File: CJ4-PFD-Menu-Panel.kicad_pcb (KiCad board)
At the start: 2 copper layers, 122.4 x 62.5 mm, 0 parts

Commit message: Some board layout work
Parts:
- added C1: 100nF, Custom_Footprints:Perfect_0402, B.Cu at (64.3, 26.5)
- added C10: 100nF, Custom_Footprints:Perfect_0402, B.Cu at (74.9, 23.7)
- added C11: 100nF, Custom_Footprints:Perfect_0402, B.Cu at (79.0, 26.2)
- added C12: 1uF, Custom_Footprints:Perfect_0402, B.Cu at (90.6, 42.4)
- added C13: 100nF, Custom_Footprints:Perfect_0402, B.Cu at (86.6, 37.9)
- added C14: 1uF, Custom_Footprints:Perfect_0402, B.Cu at (87.5, 40.4)
- added C15: 100nF, Custom_Footprints:Perfect_0402, B.Cu at (81.8, 34.4)
- added C16: 100nF, Custom_Footprints:Perfect_0402, B.Cu at (84.9, 32.0)
- added C17: 100nF, Custom_Footprints:Perfect_0402, B.Cu at (101.1, 45.1)
- added C18: 100nF, Custom_Footprints:Perfect_0402, B.Cu at (98.0, 45.1)
- added C19: 100nF, Custom_Footprints:Perfect_0402, B.Cu at (80.9, 28.3)
- added C20: 100nF, Custom_Footprints:Perfect_0402, B.Cu at (77.7, 28.3)
- added C5: 10pF, Custom_Footprints:Perfect_0402, B.Cu at (90.6, 40.4)
- added C6: 10pF, Custom_Footprints:Perfect_0402, B.Cu at (80.9, 30.3)
- added C7: 10uF, Capacitor_SMD:C_0603_1608Metric, B.Cu at (90.2, 38.1)
- added C8: 100nF, Custom_Footprints:Perfect_0402, B.Cu at (94.8, 45.1)
- added C9: 10uF, Capacitor_SMD:C_0603_1608Metric, B.Cu at (84.5, 29.8)
- added H1: Board mount, MountingHole:MountingHole_3.2mm_M3, F.Cu at (25.0, 25.0)
- added H10: JLCPCB tooling, Custom_Footprints:JLCPCB_Tooling_Hole, B.Cu at (30.0, 25.0)
- added H2: Board mount, MountingHole:MountingHole_3.2mm_M3, F.Cu at (137.0, 25.0)
- added H3: Board mount, MountingHole:MountingHole_3.2mm_M3, F.Cu at (25.0, 72.0)
- added H4: Board mount, MountingHole:MountingHole_3.2mm_M3, F.Cu at (137.0, 72.0)
- added H5: BARO encoder, Custom_Footprints:EN11-HSM1BF20_PM, F.Cu at (43.0, 52.0)
- added H6: MENU ADV and DATA encoder, Custom_Footprints:EC11E-BB24C03_PM, F.Cu at (81.0, 52.0)
- added H7: TILT and RANGE encoder, Custom_Footprints:EC11E-BB24C03_PM, F.Cu at (119.0, 52.0)
- added H8: JLCPCB tooling, Custom_Footprints:JLCPCB_Tooling_Hole, B.Cu at (132.0, 25.0)
- added H9: JLCPCB tooling, Custom_Footprints:JLCPCB_Tooling_Hole, B.Cu at (132.0, 72.0)
- added J1: USB_B_Micro, Custom_Footprints:USB_B_Mini_Amphenol_UE25BE5510H, B.Cu at (96.6, 32.1)
- added J2: Conn_01x03, Connector_PinHeader_2.54mm:PinHeader_1x03_P2.54mm_Vertical, B.Cu at (88.8, 25.0)
- added J3: BARO encoder, Connector_JST:JST_XH_B5B-XH-A_1x05_P2.50mm_Vertical, B.Cu at (48.0, 70.5)
- added J4: MENU ADV and DATA encoder, Connector_JST:JST_XH_B8B-XH-A_1x08_P2.50mm_Vertical, B.Cu at (89.8, 70.5)
- added J5: TILT and RANGE encoder, Connector_JST:JST_XH_B8B-XH-A_1x08_P2.50mm_Vertical, B.Cu at (127.2, 70.5)
- added J6: Conn_01x02, Connector_JST:JST_XH_B2B-XH-A_1x02_P2.50mm_Vertical, B.Cu at (100.8, 70.5)
- added J7: Conn_01x02, Connector_JST:JST_XH_B2B-XH-A_1x02_P2.50mm_Vertical, B.Cu at (60.8, 70.5)
- added R1: 1k, Custom_Footprints:Perfect_0402, B.Cu at (85.0, 34.1)
- added R2: 1k, Custom_Footprints:Perfect_0402, B.Cu at (74.9, 25.8)
- added R3: DNF, Resistor_SMD:R_1206_3216Metric_Pad1.30x1.75mm_HandSolder, B.Cu at (83.5, 24.4)
- added R4: 27, Resistor_SMD:R_0603_1608Metric, B.Cu at (78.5, 24.0)
- added R5: 27, Resistor_SMD:R_0603_1608Metric, B.Cu at (84.5, 27.3)
- added R6: 10k, Custom_Footprints:Perfect_0402, B.Cu at (81.8, 32.4)
- added R7: R_Small, Custom_Footprints:Perfect_0402, B.Cu at (67.5, 26.5)
- added SW1: SW_Push, Button_Switch_SMD:SW_SPST_TL3342, B.Cu at (107.0, 34.1)
- added SW10: SW_PUSH_LED, Custom_Footprints:SW_PUSH_LED_SMD, F.Cu at (60.0, 45.0)
- added SW11: SW_PUSH_LED, Custom_Footprints:SW_PUSH_LED_SMD, F.Cu at (60.0, 59.0)
- added SW12: SW_PUSH_LED, Custom_Footprints:SW_PUSH_LED_SMD, F.Cu at (102.0, 45.0)
- added SW13: SW_PUSH_LED, Custom_Footprints:SW_PUSH_LED_SMD, F.Cu at (102.0, 59.0)
- added SW2: SW_Push, Button_Switch_SMD:SW_SPST_TL3342, B.Cu at (107.0, 26.5)
- added SW3: SW_PUSH_LED, Custom_Footprints:SW_PUSH_LED_SMD, F.Cu at (39.0, 30.0)
- added SW4: SW_PUSH_LED, Custom_Footprints:SW_PUSH_LED_SMD, F.Cu at (53.0, 30.0)
- added SW5: SW_PUSH_LED, Custom_Footprints:SW_PUSH_LED_SMD, F.Cu at (67.0, 30.0)
- added SW6: SW_PUSH_LED, Custom_Footprints:SW_PUSH_LED_SMD, F.Cu at (81.0, 30.0)
- added SW7: SW_PUSH_LED, Custom_Footprints:SW_PUSH_LED_SMD, F.Cu at (95.0, 30.0)
- added SW8: SW_PUSH_LED, Custom_Footprints:SW_PUSH_LED_SMD, F.Cu at (109.0, 30.0)
- added SW9: SW_PUSH_LED, Custom_Footprints:SW_PUSH_LED_SMD, F.Cu at (123.0, 30.0)
- added TP1: TestPoint, TestPoint:TestPoint_Keystone_5000-5004_Miniature, B.Cu at (-11.5, 24.5)
- added TP2: TestPoint, TestPoint:TestPoint_Keystone_5000-5004_Miniature, B.Cu at (-22.0, 28.5)
- added TP3: TestPoint, TestPoint:TestPoint_Keystone_5000-5004_Miniature, B.Cu at (-15.8, 31.5)
- added TP4: TestPoint, TestPoint:TestPoint_Keystone_5000-5004_Miniature, B.Cu at (-11.5, 31.5)
- added TP5: TestPoint, TestPoint:TestPoint_Keystone_5000-5004_Miniature, B.Cu at (-15.8, 24.5)
- added U1: AMS1117-3.3, Package_TO_SOT_SMD:SOT-223-3_TabPin2, B.Cu at (107.6, 42.0)
- added U2: DM13A, Package_SO:SSOP-24_3.9x8.7mm_P0.635mm, B.Cu at (57.2, 29.2)
- added U5: W25Q128JVS, Package_SO:SOIC-8_5.23x5.23mm_P1.27mm, B.Cu at (96.3, 26.1)
- added U6: RP2040, Custom_Footprints:QFN-56-1EP_7x7mm_P0.4mm_EP3.2x3.2mm, B.Cu at (96.8, 39.4)
- added Y1: X322512MSB4SI, Crystal:Crystal_SMD_3225-4Pin_3.2x2.5mm, B.Cu at (89.2, 34.6)
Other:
- board size 122.4 x 62.5 mm -> 122 x 57 mm

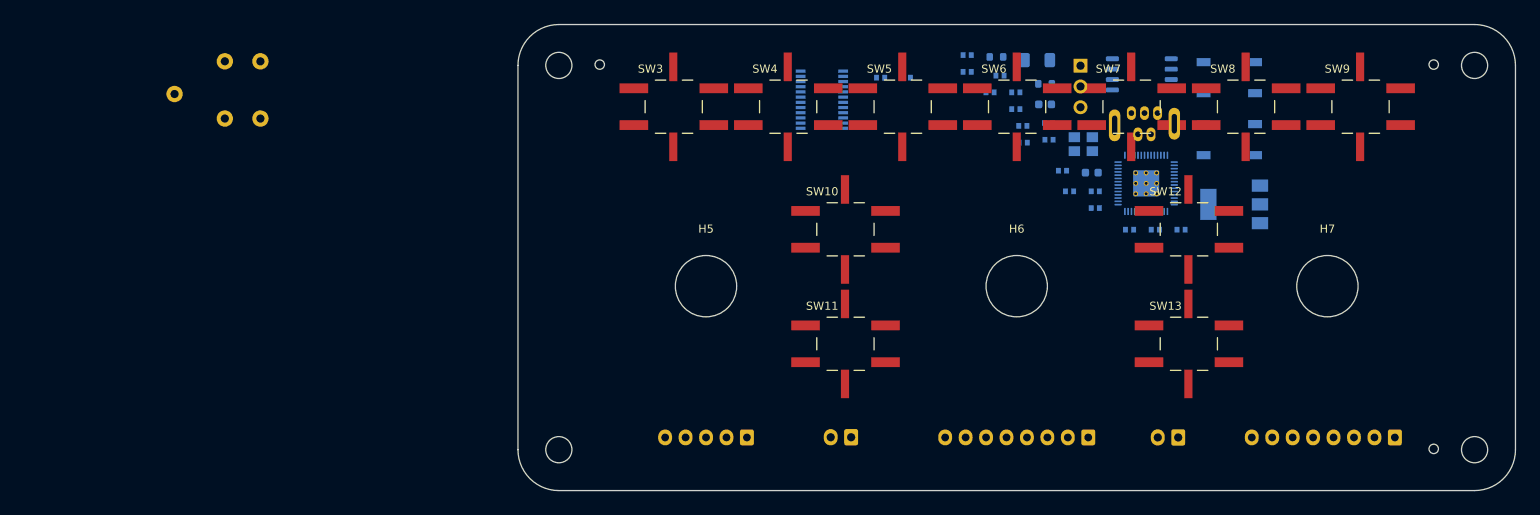
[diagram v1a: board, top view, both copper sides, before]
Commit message: Redo RP2040 layout
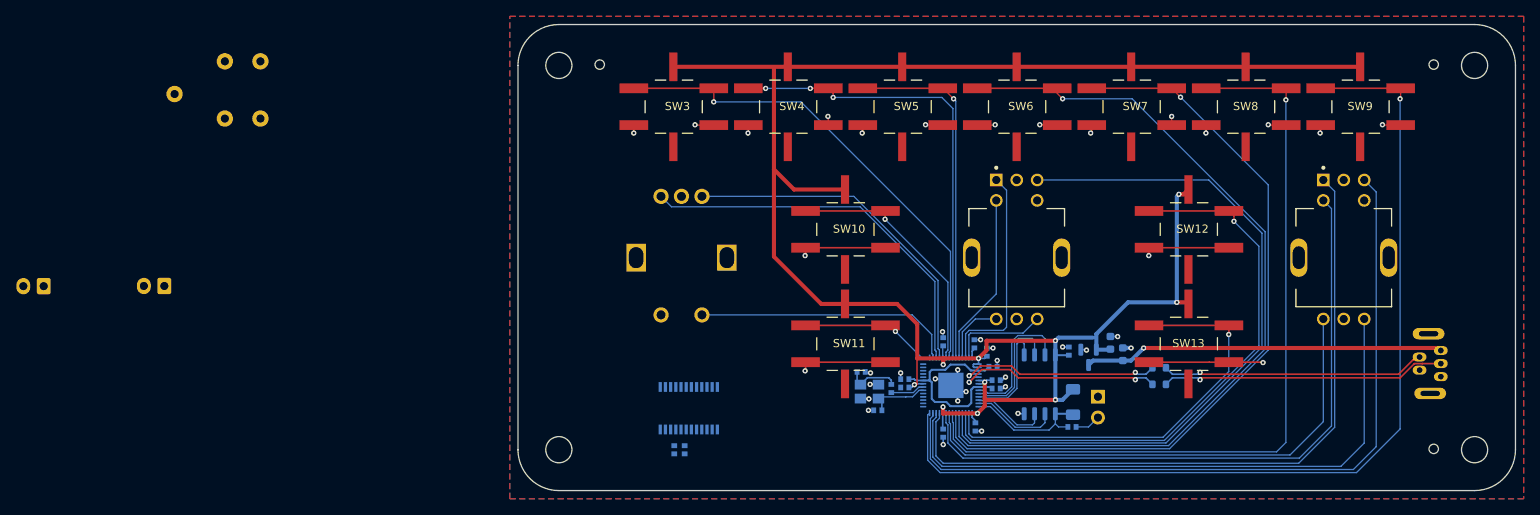
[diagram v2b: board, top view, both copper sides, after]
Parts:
- removed C14: 1uF, Custom_Footprints:Perfect_0402
- removed H5: BARO encoder, Custom_Footprints:EN11-HSM1BF20_PM
- removed H6: MENU ADV and DATA encoder, Custom_Footprints:EC11E-BB24C03_PM
- removed H7: TILT and RANGE encoder, Custom_Footprints:EC11E-BB24C03_PM
- removed J2: Conn_01x03, Connector_PinHeader_2.54mm:PinHeader_1x03_P2.54mm_Vertical
- removed J4: MENU ADV and DATA encoder, Connector_JST:JST_XH_B8B-XH-A_1x08_P2.50mm_Vertical
- removed J5: TILT and RANGE encoder, Connector_JST:JST_XH_B8B-XH-A_1x08_P2.50mm_Vertical
- removed J7: Conn_01x02, Connector_JST:JST_XH_B2B-XH-A_1x02_P2.50mm_Vertical
- removed R4: 27, Resistor_SMD:R_0603_1608Metric
- removed SW1, SW2: SW_Push, Button_Switch_SMD:SW_SPST_TL3342
- removed U5: W25Q128JVS, Package_SO:SOIC-8_5.23x5.23mm_P1.27mm
- added ENC1: BARO encoder, Custom_Footprints:EN11-HSM1BF20_THT, F.Cu at (40.0, 48.5)
- added ENC2: MENU ADV and DATA encoder, Custom_Footprints:ALPS-EC11EBB24C03-0, F.Cu at (81.0, 48.5)
- added ENC3: TILT and RANGE encoder, Custom_Footprints:ALPS-EC11EBB24C03-0, F.Cu at (121.0, 48.5)
- added J8: Conn_01x02, Connector_JST:JST_XH_B2B-XH-A_1x02_P2.50mm_Vertical, B.Cu at (-38.0, 52.0)
- added U7: RP2040, Custom_Footprints:QFN57P40_700X700X90L40X18T310N, B.Cu at (72.9, 64.1)
- C10, C11, C13, C15, C16, C17, C18, C19, C20: value 100nF -> 1uF
- C7, C9: value 10uF -> 1uF
- J1: value USB_B_Micro -> Conn_01x02; footprint Custom_Footprints:USB_B_Mini_Amphenol_UE25BE5510H -> Connector_JST:JST_XH_B2B-XH-A_1x02_P2.50mm_Vertical
- J3: value BARO encoder -> Conn_01x02; footprint Connector_JST:JST_XH_B5B-XH-A_1x05_P2.50mm_Vertical -> Connector_PinHeader_2.54mm:PinHeader_1x02_P2.54mm_Vertical
- J6: value Conn_01x02 -> USB_B_Micro; footprint Connector_JST:JST_XH_B2B-XH-A_1x02_P2.50mm_Vertical -> Custom_Footprints:USB_B_Mini_Amphenol_UE25BE5510H
- R1: value 1k -> R_Small
- R3: value DNF -> 1k; footprint Resistor_SMD:R_1206_3216Metric_Pad1.30x1.75mm_HandSolder -> Custom_Footprints:Perfect_0402
- R5: value 27 -> DNF; footprint Resistor_SMD:R_0603_1608Metric -> Resistor_SMD:R_1206_3216Metric_Pad1.30x1.75mm_HandSolder
- R6: value 10k -> 27; footprint Custom_Footprints:Perfect_0402 -> Resistor_SMD:R_0603_1608Metric
- R7: value R_Small -> 27; footprint Custom_Footprints:Perfect_0402 -> Resistor_SMD:R_0603_1608Metric
- U1: value AMS1117-3.3 -> DM13A; footprint Package_TO_SOT_SMD:SOT-223-3_TabPin2 -> Package_SO:SSOP-24_3.9x8.7mm_P0.635mm
- U2: value DM13A -> XC6206P332MR; footprint Package_SO:SSOP-24_3.9x8.7mm_P0.635mm -> Package_TO_SOT_SMD:SOT-23
- U6: value RP2040 -> W25Q128JVS; footprint Custom_Footprints:QFN-56-1EP_7x7mm_P0.4mm_EP3.2x3.2mm -> Package_SO:SOIC-8_5.23x5.23mm_P1.27mm
- moved J1 121.5 mm to (-23.2, 52.0)
- moved U1 71.2 mm to (40.9, 66.9), turned to 90 degrees
- moved R1 59.5 mm to (39.1, 72.0), turned to 90 degrees
- moved C1 51.4 mm to (40.4, 72.0), turned to 90 degrees
- moved R7 47.1 mm to (98.4, 62.0)
- moved U2 45.3 mm to (89.8, 60.7), turned to -90 degrees
- moved R3 45.1 mm to (87.8, 69.2), turned to 0 degrees
- moved J3 43.2 mm to (90.9, 65.5)
- moved C19 41.2 mm to (75.9, 69.2), turned to -90 degrees
- moved Y1 40.0 mm to (63.0, 64.9), turned to 0 degrees
- moved R2 39.8 mm to (65.7, 64.5), turned to 90 degrees
- moved R5 39.1 mm to (87.9, 66.2), turned to -90 degrees
- moved C17 38.3 mm to (72.0, 70.0), turned to -90 degrees
- moved C11 38.3 mm to (78.5, 64.5), turned to 0 degrees
- moved C10 38.2 mm to (78.1, 61.8), turned to 0 degrees
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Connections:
- J1 pad 1: VBUS -> /MASTER_WARNING
- J1 pad 2: /RP2040/USB_D- -> GND
- J3 pad 1: /BARO_A -> GND
- J3 pad 2: GND -> /RP2040/~{USB_BOOT}
- J6 pad 1: /MASTER_WARNING -> VBUS
- J6 pad 2: GND -> /RP2040/USB_D-
- R1 pad 1: /RP2040/QSPI_SS -> /REXT
- R1 pad 2: /RP2040/~{USB_BOOT} -> GND
- R3 pad 1: +3V3 -> /RP2040/QSPI_SS
- R3 pad 2: /RP2040/QSPI_SS -> /RP2040/~{USB_BOOT}
- R5 pad 1: /RP2040/USB_D- -> +3V3
- R5 pad 2: /RP2040/USB_D-R -> /RP2040/QSPI_SS
- R6 pad 1: /RP2040/RUN -> /RP2040/USB_D+
- R6 pad 2: +3V3 -> /RP2040/USB_D_R+
- R7 pad 1: Net-(R7-Pad1) -> /RP2040/USB_D-
- R7 pad 2: GND -> /RP2040/USB_D_R-
- U1 pad 2: +3V3 -> /LED_DIN
- U1 pad 3: VBUS -> /LED_CLOCK
- U2 pad 2: /LED_DIN -> +3V3
- U2 pad 3: /LED_CLOCK -> VBUS
- U6 pad 1: +3V3 -> /RP2040/QSPI_SS
- U6 pad 2: /LED_DIN -> /RP2040/QSPI_SD1
- U6 pad 3: /LED_CLOCK -> /RP2040/QSPI_SD2
- U6 pad 4: /LED_LATCH -> GND
- U6 pad 5: /BRIGHTNESS -> /RP2040/QSPI_SD0
- U6 pad 6: /MASTER_WARNING -> /RP2040/QSPI_SCLK
- U6 pad 7: /MASTER_CAUTION -> /RP2040/QSPI_SD3
- U6 pad 8: /NAV -> +3V3
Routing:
- net +3V3: track 0.00 -> 246.4 mm, vias 0 -> 10
- net /TFC: track 0.00 -> 118.0 mm, vias 0 -> 1
- net /ET: track 0.00 -> 102.8 mm, vias 0 -> 1
- net /TERRWX: track 0.00 -> 98.1 mm, vias 0 -> 1
- net /RANGE_B': track 0.00 -> 95.2 mm
- net /FRMT: track 0.00 -> 93.4 mm, vias 0 -> 1
- net /DATA_B': track 0.00 -> 88.7 mm
- net /TILT_A': track 0.00 -> 87.2 mm
- net GND: track 0.00 -> 86.8 mm, vias 0 -> 40
- net /AUTO_TILT_BTN: track 0.00 -> 81.1 mm
- net /RANGE_B: track 0.00 -> 75.1 mm
- net /RADAR_MENU: track 0.00 -> 71.4 mm, vias 0 -> 1
- net /TILT_A: track 0.00 -> 64.0 mm
- net /NAV: track 0.00 -> 61.0 mm, vias 0 -> 1
- net /PFD_MENU: track 0.00 -> 56.9 mm, vias 0 -> 3
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- added copper zone on B.Cu, net GND
- added copper zone on F.Cu, net GND

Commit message: Fully routed!
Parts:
- J1, J8: footprint Connector_JST:JST_XH_B2B-XH-A_1x02_P2.50mm_Vertical -> Connector_JST:JST_XH_B3B-XH-A_1x03_P2.50mm_Vertical
- SW10, SW11, SW12, SW13, SW3, SW4, SW5, SW6, SW7, SW8, SW9: footprint Custom_Footprints:SW_PUSH_LED_SMD -> Custom_Footprints:SW_PUSH_LED_THT
- moved TP2 94.3 mm to (61.1, 73.2)
- moved TP1 91.7 mm to (66.2, 73.2)
- moved TP3 83.1 mm to (56.0, 73.2)
- moved TP5 79.4 mm to (46.7, 73.4)
- moved TP4 78.1 mm to (58.3, 66.5)
- moved J8 64.1 mm to (25.4, 42.8), turned to 90 degrees
- moved J1 48.7 mm to (25.4, 54.4), turned to 90 degrees
- moved C1 15.5 mm to (51.7, 61.5)
- moved R1 15.5 mm to (50.4, 61.5)
- moved U1 6.40 mm to (47.2, 66.2)
- moved J6 4.70 mm to (130.0, 65.9)
- moved C6 2.61 mm to (60.2, 64.4), turned to -90 degrees
- moved R6 2.55 mm to (98.2, 66.5)
- moved R7 2.55 mm to (98.2, 64.5)
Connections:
- J1 pad 1: /MASTER_WARNING -> /LED_CAUTION
- J1 pad 2: GND -> /MASTER_WARNING
- J8 pad 1: /MASTER_CAUTION -> /LED_WARNING
- J8 pad 2: GND -> /MASTER_CAUTION
- U1 pad 10: /LED_TERRWX -> /LED_WARNING
- U1 pad 11: /LED_TFC -> /LED_CAUTION
- U1 pad 12: /LED_CCP_MENU -> /LED_NAV
- U1 pad 13: /LED_TAWS_MENU -> /LED_PFD_MENU
- U1 pad 14: /LED_RADAR_MENU -> /LED_ESC
- U1 pad 15: /LED_REFS_MENU -> /LED_ET
- U1 pad 16: /LED_MASTER_CAUTION -> /LED_FRMT
- U1 pad 17: /LED_MASTER_WARNING -> /LED_TERRWX
- U1 pad 18: unconnected-(U1-Pad18) -> /LED_RADAR_MENU
- U1 pad 19: unconnected-(U1-Pad19) -> /LED_REFS_MENU
- U1 pad 20: unconnected-(U1-Pad20) -> /LED_CCP_MENU
- U1 pad 5: /LED_NAV -> /LED_TAWS_MENU
- U1 pad 6: /LED_PFD_MENU -> /LED_TFC
- U1 pad 7: /LED_ESC -> unconnected-(U1-Pad7)
- U1 pad 8: /LED_ET -> unconnected-(U1-Pad8)
- U1 pad 9: /LED_FRMT -> unconnected-(U1-Pad9)
- U7 pad 11: /TILT_A' -> /TILT_A
- U7 pad 12: /RANGE_B -> /RANGE_B'
- U7 pad 13: /RANGE_B' -> /RANGE_B
- U7 pad 15: /RP2040/GPIO12 -> /LED_DIN
- U7 pad 16: /RP2040/GPIO13 -> /LED_CLOCK
- U7 pad 17: /RP2040/GPIO14 -> /LED_LATCH
- U7 pad 18: /RP2040/GPIO15 -> /BRIGHTNESS
- U7 pad 27: /RP2040/GPIO16 -> /MASTER_WARNING
- U7 pad 28: /RP2040/GPIO17 -> /MASTER_CAUTION
- U7 pad 29: /REFS_MENU -> /STD_BTN
- U7 pad 3: /RADAR_MENU -> /DATA_B'
- U7 pad 30: /STD_BTN -> /REFS_MENU
- U7 pad 31: /BARO_B -> /CCP_MENU
- U7 pad 34: /CCP_MENU -> /BARO_B
- U7 pad 38: /SELECT_BTN -> /MENU_ADV_A'
- U7 pad 39: /MENU_ADV_A -> /SELECT_BTN
- U7 pad 4: /DATA_B' -> /RADAR_MENU
- U7 pad 40: /MENU_ADV_A' -> /MENU_ADV_A
- U7 pad 8: /TILT_A -> /TILT_A'
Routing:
- net /LED_TFC: track 0.00 -> 116.5 mm, vias 0 -> 2
- net /LED_TERRWX: track 0.00 -> 88.9 mm, vias 0 -> 4
- net /LED_RADAR_MENU: track 0.00 -> 83.4 mm, vias 0 -> 4
- net /LED_FRMT: track 0.00 -> 76.1 mm, vias 0 -> 4
- net /LED_TAWS_MENU: track 0.00 -> 69.2 mm, vias 0 -> 2
- net GND: track 86.8 -> 23.4 mm, vias 40 -> 26
- net /LED_ET: track 0.00 -> 63.2 mm, vias 0 -> 4
- net /MASTER_CAUTION: track 0.00 -> 58.4 mm, vias 0 -> 2
- net /LED_ESC: track 0.00 -> 50.2 mm, vias 0 -> 2
- net /MASTER_WARNING: track 0.00 -> 48.3 mm, vias 0 -> 2
- net /LED_WARNING: track 0.00 -> 42.3 mm
- net /LED_NAV: track 0.00 -> 39.9 mm
- net /LED_PFD_MENU: track 0.00 -> 37.2 mm, vias 0 -> 2
- net /LED_CLOCK: track 0.00 -> 36.7 mm
- net /LED_LATCH: track 0.00 -> 33.1 mm
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
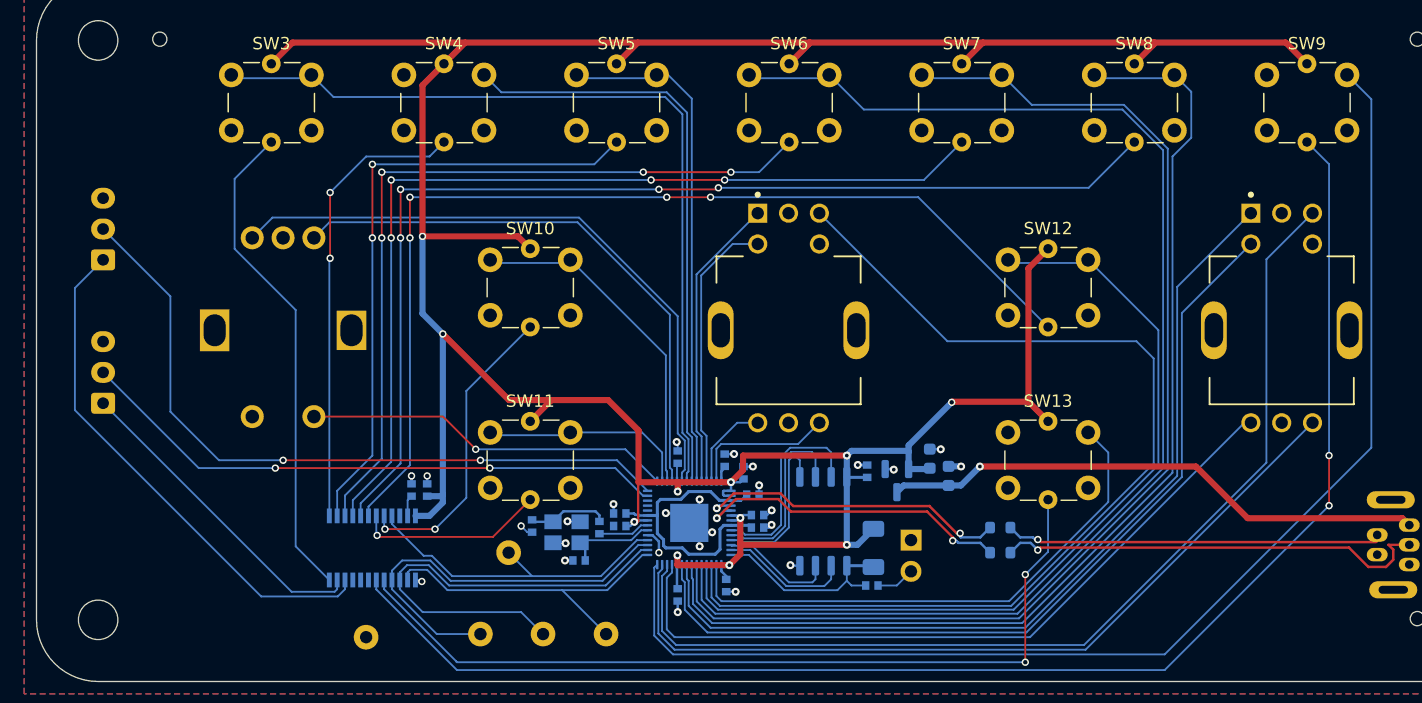
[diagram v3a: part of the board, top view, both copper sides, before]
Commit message: Update external button connector, 3d models
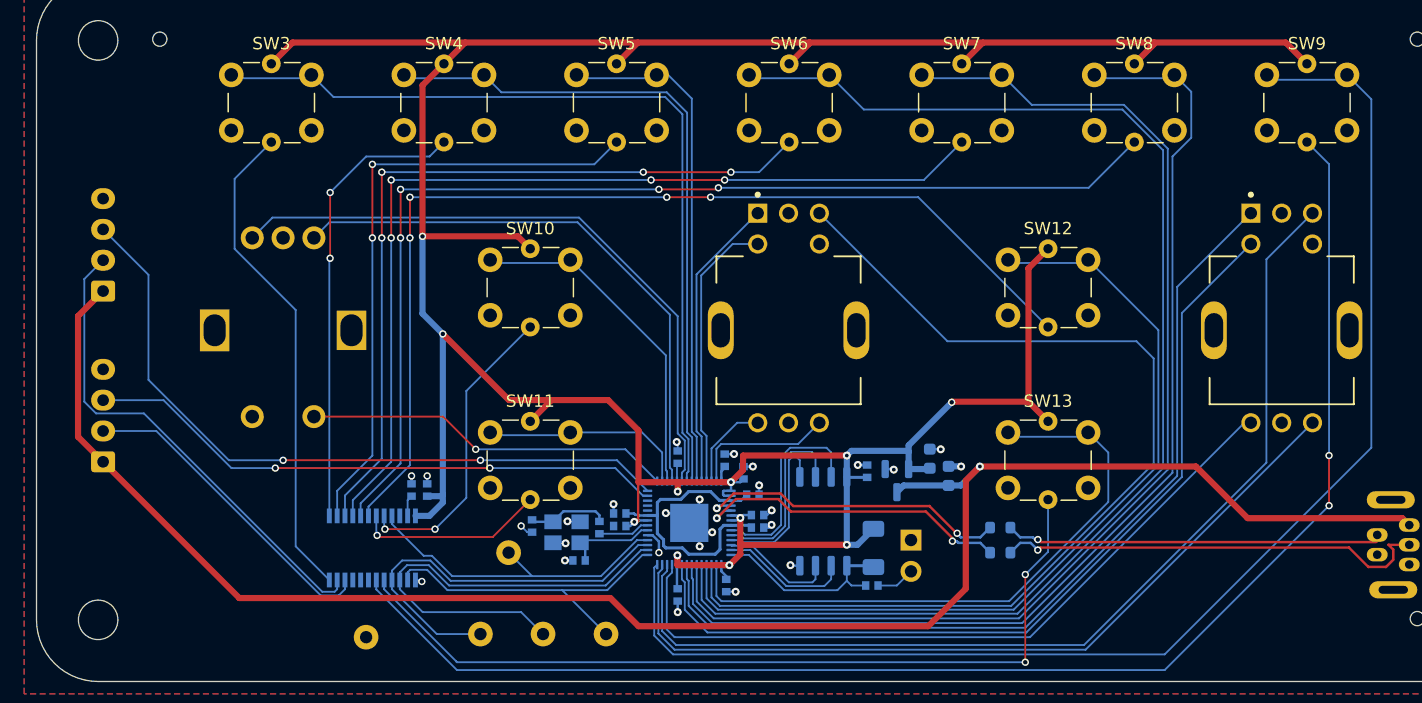
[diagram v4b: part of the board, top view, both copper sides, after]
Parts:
- J1, J8: footprint Connector_JST:JST_XH_B3B-XH-A_1x03_P2.50mm_Vertical -> Connector_JST:JST_XH_B4B-XH-A_1x04_P2.50mm_Vertical
- U7: footprint Custom_Footprints:QFN57P40_700X700X90L40X18T310N -> Custom_Footprints:QFN56P40_700X700X90L40X18T310N
- moved J1 4.75 mm to (25.4, 59.2)
- moved J8 2.53 mm to (25.4, 45.3)
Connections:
- C7 pad 1: VBUS -> +5V
- J1 pad 1: /LED_CAUTION -> +5V
- J1 pad 2: /MASTER_WARNING -> /LED_CAUTION
- J1 pad 3: GND -> /MASTER_WARNING
- J6 pad 1: VBUS -> +5V
- J8 pad 1: /LED_WARNING -> +5V
- J8 pad 2: /MASTER_CAUTION -> /LED_WARNING
- J8 pad 3: GND -> /MASTER_CAUTION
- U1 pad 10: /LED_WARNING -> /LED_CAUTION
- U1 pad 11: /LED_CAUTION -> /LED_WARNING
- U2 pad 3: VBUS -> +5V
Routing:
- net +5V: track 0.00 -> 147.1 mm, vias 0 -> 1
- net VBUS: track 44.4 -> 0.00 mm, vias 1 -> 0
- net /TFC: track 102.7 -> 109.5 mm
- net /TAWS_MENU: track 44.2 -> 51.0 mm
- net /PFD_MENU: track 47.8 -> 54.5 mm
- net /LED_WARNING: track 42.3 -> 39.8 mm
- net /MASTER_WARNING: track 48.3 -> 47.4 mm
- net /MASTER_CAUTION: track 58.4 -> 57.9 mm
